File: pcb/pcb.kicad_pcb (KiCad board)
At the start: 2 copper layers, 63.8 x 43.2 mm, 34 parts, among them J1 BAT+, J10 GRN, J11 RED, J12 Load Cell, J2 BAT-, J3 Battery, J4 DS18B20, J5 TMP+, J6 TMPO, J7 TMP-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

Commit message: pcb-1.0.0-rc.4
Just a few final tweaks—labeling, adding a capacitor across USB
in for filtering.
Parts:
- added ?: , Symbols:OSHW-Logo2_7.3x6mm_SilkScreen, B.Cu at (125.2, 97.3)
- added C6: 1uF, Capacitors_SMD:C_0805, F.Cu at (142.1, 73.8)
- renumbered U1 to CN1, U3 to CN2, U4 to CN3, U5 to U1
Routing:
- net /USB+: track 77.3 -> 78.9 mm
- net /GND: track 65.9 -> 66.9 mm, vias 13 -> 14
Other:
- board text added: "1.0.0-rc.4"
- board text removed: "1.0.0-rc.3"
- board text removed: "OSHW"

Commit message: More capacitance! More ground pour!
Per recommendations. The ADC trace is long and very low-current,
and needs some smoothing for EMI reasons. The ground pour is bigger
to reduce the number of long traces to ground.
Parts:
- added C7: 100nF, Capacitors_SMD:C_0805, F.Cu at (141.1, 97.8)
- C6: value 1uF -> 100nF
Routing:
- net /GND: track 66.9 -> 52.1 mm, vias 14 -> 16
- net /ADC: track 48.3 -> 49.5 mm
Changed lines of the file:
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@@
 (kicad_pcb (version 4) (host pcbnew 4.0.7-e2-6376~58~ubuntu16.04.1)
   (general
-    (links 68)
+    (links 70)
     (no_connects 0)
-    (area 99.863999 58.638 182.188 114.438001)
+    (area 106.162999 65.462999 170.113001 108.813001)
     (thickness 1.6)
     (drawings 21)
-    (tracks 388)
+    (tracks 394)
     (zones 0)
-    (modules 36)
+    (modules 37)
     (nets 25)
   )
@@
       (effects (font (size 1 1) (thickness 0.15)))
     )
-    (fp_text value 1uF (at 5.207 0 270) (layer F.SilkS)
+    (fp_text value 100nF (at 5.842 0 270) (layer F.SilkS)
       (effects (font (size 1 1) (thickness 0.15)))
     )
@@
       (xy -0.113933 2.757629) (xy -0.013056 2.757714) (xy 0 2.757714) (xy 0.10391 2.757652)) (layer B.SilkS) (width 0.01))
   )
+  (module Capacitors_SMD:C_0805 (layer F.Cu)
+    (at 141.097 97.79 90)
+    (descr "Capacitor SMD 0805, reflow soldering, AVX (see smccp.pdf)")
+    (tags "capacitor 0805")
+    (attr smd)
+    (fp_text reference C7 (at 0.381 2.032 180) (layer F.SilkS)
+      (effects (font (size 1 1) (thickness 0.15)))
+    )
+    (fp_text value 100nF (at 1.905 3.429 180) (layer F.SilkS)
+      (effects (font (size 1 1) (thickness 0.15)))
+    )
+    (fp_text user %R (at 0.381 2.032 180) (layer F.Fab)
+      (effects (font (size 1 1) (thickness 0.15)))
+    )
+    (fp_line (start -1 0.62) (end -1 -0.62) (layer F.Fab) (width 0.1))
+    (fp_line (start 1 0.62) (end -1 0.62) (layer F.Fab) (width 0.1))
+    (fp_line (start 1 -0.62) (end 1 0.62) (layer F.Fab) (width 0.1))
+    (fp_line (start -1 -0.62) (end 1 -0.62) (layer F.Fab) (width 0.1))
+    (fp_line (start 0.5 -0.85) (end -0.5 -0.85) (layer F.SilkS) (width 0.12))
+    (fp_line (start -0.5 0.85) (end 0.5 0.85) (layer F.SilkS) (width 0.12))
+    (fp_line (start -1.75 -0.88) (end 1.75 -0.88) (layer F.CrtYd) (width 0.05))
+    (fp_line (start -1.75 -0.88) (end -1.75 0.87) (layer F.CrtYd) (width 0.05))
+    (fp_line (start 1.75 0.87) (end 1.75 -0.88) (layer F.CrtYd) (width 0.05))
+    (fp_line (start 1.75 0.87) (end -1.75 0.87) (layer F.CrtYd) (width 0.05))
+    (pad 1 smd rect (at -1 0 90) (size 1 1.25) (layers F.Cu F.Paste F.Mask)
+      (net 13 /ADC))
+    (pad 2 smd rect (at 1 0 90) (size 1 1.25) (layers F.Cu F.Paste F.Mask)
+      (net 9 /GND))
+    (model Capacitors_SMD.3dshapes/C_0805.wrl
+      (at (xyz 0 0 0))
+      (scale (xyz 1 1 1))
+      (rotate (xyz 0 0 0))
+    )
+  )
   (gr_text - (at 135.128 83.566) (layer F.SilkS)
     (effects (font (size 1.5 1.5) (thickness 0.3)) (justify mirror))
@@
   (segment (start 136.636 95.996) (end 138.938 98.298) (width 0.4) (layer F.Cu) (net 8))
   (segment (start 141.108 105.416) (end 141.108 105.294) (width 0.4) (layer F.Cu) (net 8))
+  (segment (start 138.684 93.996) (end 138.795 93.996) (width 0.25) (layer F.Cu) (net 9) (status C00000))
+  (segment (start 138.795 93.996) (end 139.7 93.091) (width 0.25) (layer F.Cu) (net 9) (status 400000))
+  (via (at 139.7 93.091) (size 0.6) (drill 0.4) (layers F.Cu B.Cu) (net 9))
+  (segment (start 150.556 100.838) (end 150.876 100.838) (width 0.25) (layer F.Cu) (net 9) (status C00000))
+  (segment (start 150.876 100.838) (end 151.384 100.33) (width 0.25) (layer F.Cu) (net 9) (status 400000))
+  (via (at 151.384 100.33) (size 0.6) (drill 0.4) (layers F.Cu B.Cu) (net 9))
+  (segment (start 141.097 96.79) (end 139.938 96.79) (width 0.25) (layer F.Cu) (net 9))
+  (via (at 139.827 96.901) (size 0.6) (drill 0.4) (layers F.Cu B.Cu) (net 9))
+  (segment (start 139.938 96.79) (end 139.827 96.901) (width 0.25) (layer F.Cu) (net 9))
   (segment (start 142.113 72.787) (end 142.113 71.755) (width 0.4) (layer F.Cu) (net 9))
   (via (at 142.113 71.755) (size 0.6) (drill 0.4) (layers F.Cu B.Cu) (net 9))
@@
   (segment (start 133.669 107.618) (end 133.858 107.807) (width 0.4) (layer F.Cu) (net 9))
   (segment (start 138.684 93.996) (end 138.728 93.996) (width 0.4) (layer F.Cu) (net 9))
-  (segment (start 138.728 93.996) (end 141.108 91.616) (width 0.4) (layer F.Cu) (net 9))
   (segment (start 131.064 107.618) (end 131.142 107.618) (width 0.4) (layer F.Cu) (net 9))
   (via (at 132.207 106.553) (size 0.6) (drill 0.4) (layers F.Cu B.Cu) (net 9))
@@
   (segment (start 121.793 84.074) (end 121.793 85.156) (width 0.4) (layer F.Cu) (net 9) (status 20))
   (via (at 121.793 84.074) (size 0.6) (drill 0.4) (layers F.Cu B.Cu) (net 9))
-  (segment (start 150.556 100.838) (end 151.638 100.838) (width 0.25) (layer F.Cu) (net 9) (status 10))
-  (segment (start 140.081 99.949) (end 137.922 99.949) (width 0.25) (layer B.Cu) (net 9))
-  (segment (start 140.97 100.838) (end 140.081 99.949) (width 0.25) (layer B.Cu) (net 9))
-  (segment (start 151.638 100.838) (end 140.97 100.838) (width 0.25) (layer B.Cu) (net 9))
-  (via (at 151.638 100.838) (size 0.6) (drill 0.4) (layers F.Cu B.Cu) (net 9))
   (segment (start 126 99.314) (end 125.349 99.314) (width 0.4) (layer F.Cu) (net 9) (status 10))
   (via (at 124.968 98.933) (size 0.6) (drill 0.4) (layers F.Cu B.Cu) (net 9))
@@
   (via (at 118.872 93.218) (size 0.6) (drill 0.4) (layers F.Cu B.Cu) (net 12))
   (segment (start 120.396 93.218) (end 118.872 93.218) (width 0.25) (layer B.Cu) (net 12))
+  (segment (start 141.605 99.822) (end 141.605 99.298) (width 0.25) (layer F.Cu) (net 13))
+  (segment (start 141.605 99.298) (end 141.097 98.79) (width 0.25) (layer F.Cu) (net 13))
   (segment (start 145.857 100.838) (end 145.857 100.518) (width 0.25) (layer F.Cu) (net 13) (status 30))
   (segment (start 145.857 100.518) (end 145.161 99.822) (width 0.25) (layer F.Cu) (net 13) (status 10))
-  (segment (start 145.161 99.822) (end 140.589 99.822) (width 0.25) (layer F.Cu) (net 13))
+  (segment (start 145.161 99.822) (end 141.605 99.822) (width 0.25) (layer F.Cu) (net 13))
+  (segment (start 141.605 99.822) (end 140.589 99.822) (width 0.25) (layer F.Cu) (net 13))
   (segment (start 119.253 105.537) (end 113.0935 105.537) (width 0.25) (layer B.Cu) (net 13))
   (segment (start 113.0935 105.537) (end 111.8235 104.267) (width 0.25) (layer B.Cu) (net 13))
@@
     (polygon
       (pts
-        (xy 165.989 82.296) (xy 165.989 93.091) (xy 162.179 93.091) (xy 162.179 91.694) (xy 143.51 91.694)
-        (xy 142.24 93.218) (xy 139.954 95.758) (xy 138.303 97.409) (xy 138.303 101.6) (xy 138.303 107.061)
-        (xy 129.032 107.061) (xy 123.571 101.6) (xy 112.522 101.6) (xy 112.522 98.806) (xy 112.522 69.088)
-        (xy 143.51 69.088)
+        (xy 165.989 82.296) (xy 165.989 93.091) (xy 165.989 100.711) (xy 138.303 100.711) (xy 138.303 107.061)
+        (xy 129.032 107.061) (xy 123.571 101.6) (xy 112.522 101.6) (xy 112.522 69.088) (xy 143.51 69.088)
       )
     )

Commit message: pcb-1.0.0-rc.5, blog post
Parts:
- added H1: MountingHole_2.2mm_M2, Mounting_Holes:MountingHole_2.2mm_M2, F.Cu at (114.8, 68.1)
- added H2: MountingHole_2.2mm_M2, Mounting_Holes:MountingHole_2.2mm_M2, F.Cu at (167.5, 106.2)
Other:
- board text added: "1.0.0-rc.5"
- board text removed: "1.0.0-rc.4"
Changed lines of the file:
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@@
     (tracks 394)
     (zones 0)
-    (modules 37)
+    (modules 39)
     (nets 25)
   )
@@
   (title_block
     (title "Pendulum PCB")
-    (date 2018-06-25)
-    (rev 1.0.0-rc.4)
+    (date 2018-06-26)
+    (rev 1.0.0-rc.5)
   )
   (layers
@@
     (add_net "Net-(R6-Pad2)")
     (add_net "Net-(R7-Pad2)")
+  )
+  (module Mounting_Holes:MountingHole_2.2mm_M2 (layer F.Cu)
+    (at 167.513 106.172)
+    (descr "Mounting Hole 2.2mm, no annular, M2")
+    (tags "mounting hole 2.2mm no annular m2")
+    (fp_text reference H2 (at 0 -2.159) (layer F.SilkS)
+      (effects (font (size 1 1) (thickness 0.15)))
+    )
+    (fp_text value MountingHole_2.2mm_M2 (at 0 3.2) (layer F.Fab)
+      (effects (font (size 1 1) (thickness 0.15)))
+    )
+    (fp_circle (center 0 0) (end 2.2 0) (layer Cmts.User) (width 0.15))
+    (fp_circle (center 0 0) (end 2.45 0) (layer F.CrtYd) (width 0.05))
+    (pad 1 np_thru_hole circle (at 0 0) (size 2.2 2.2) (drill 2.2) (layers *.Cu *.Mask))
   )
   (module Resistors_SMD:R_0805 (layer F.Cu)
@@
     )
   )
+  (module Mounting_Holes:MountingHole_2.2mm_M2 (layer F.Cu)
+    (at 114.808 68.072)
+    (descr "Mounting Hole 2.2mm, no annular, M2")
+    (tags "mounting hole 2.2mm no annular m2")
+    (fp_text reference H1 (at 0 2.286) (layer F.SilkS)
+      (effects (font (size 1 1) (thickness 0.15)))
+    )
+    (fp_text value MountingHole_2.2mm_M2 (at 0.254 -3.556) (layer F.Fab)
+      (effects (font (size 1 1) (thickness 0.15)))
+    )
+    (fp_circle (center 0 0) (end 2.2 0) (layer Cmts.User) (width 0.15))
+    (fp_circle (center 0 0) (end 2.45 0) (layer F.CrtYd) (width 0.05))
+    (pad 1 np_thru_hole circle (at 0 0) (size 2.2 2.2) (drill 2.2) (layers *.Cu *.Mask))
+  )
   (gr_text - (at 135.128 83.566) (layer F.SilkS)
     (effects (font (size 1.5 1.5) (thickness 0.3)) (justify mirror))
@@
     (arrow2b (pts (xy 100.138 111.738) (xy 101.264504 111.151579)))
   )
-  (gr_text 1.0.0-rc.4 (at 129.286 97.282 270) (layer B.SilkS)
+  (gr_text 1.0.0-rc.5 (at 129.286 97.282 270) (layer B.SilkS)
     (effects (font (size 1 1) (thickness 0.15)) (justify mirror))
   )
@@
   (segment (start 136.636 95.996) (end 138.938 98.298) (width 0.4) (layer F.Cu) (net 8))
   (segment (start 141.108 105.416) (end 141.108 105.294) (width 0.4) (layer F.Cu) (net 8))
-  (segment (start 138.684 93.996) (end 138.795 93.996) (width 0.25) (layer F.Cu) (net 9) (status C00000))
-  (segment (start 138.795 93.996) (end 139.7 93.091) (width 0.25) (layer F.Cu) (net 9) (status 400000))
+  (segment (start 138.684 93.996) (end 138.795 93.996) (width 0.25) (layer F.Cu) (net 9))
+  (segment (start 138.795 93.996) (end 139.7 93.091) (width 0.25) (layer F.Cu) (net 9))
   (via (at 139.7 93.091) (size 0.6) (drill 0.4) (layers F.Cu B.Cu) (net 9))
-  (segment (start 150.556 100.838) (end 150.876 100.838) (width 0.25) (layer F.Cu) (net 9) (status C00000))
-  (segment (start 150.876 100.838) (end 151.384 100.33) (width 0.25) (layer F.Cu) (net 9) (status 400000))
+  (segment (start 150.556 100.838) (end 150.876 100.838) (width 0.25) (layer F.Cu) (net 9))
+  (segment (start 150.876 100.838) (end 151.384 100.33) (width 0.25) (layer F.Cu) (net 9))
   (via (at 151.384 100.33) (size 0.6) (drill 0.4) (layers F.Cu B.Cu) (net 9))
   (segment (start 141.097 96.79) (end 139.938 96.79) (width 0.25) (layer F.Cu) (net 9))

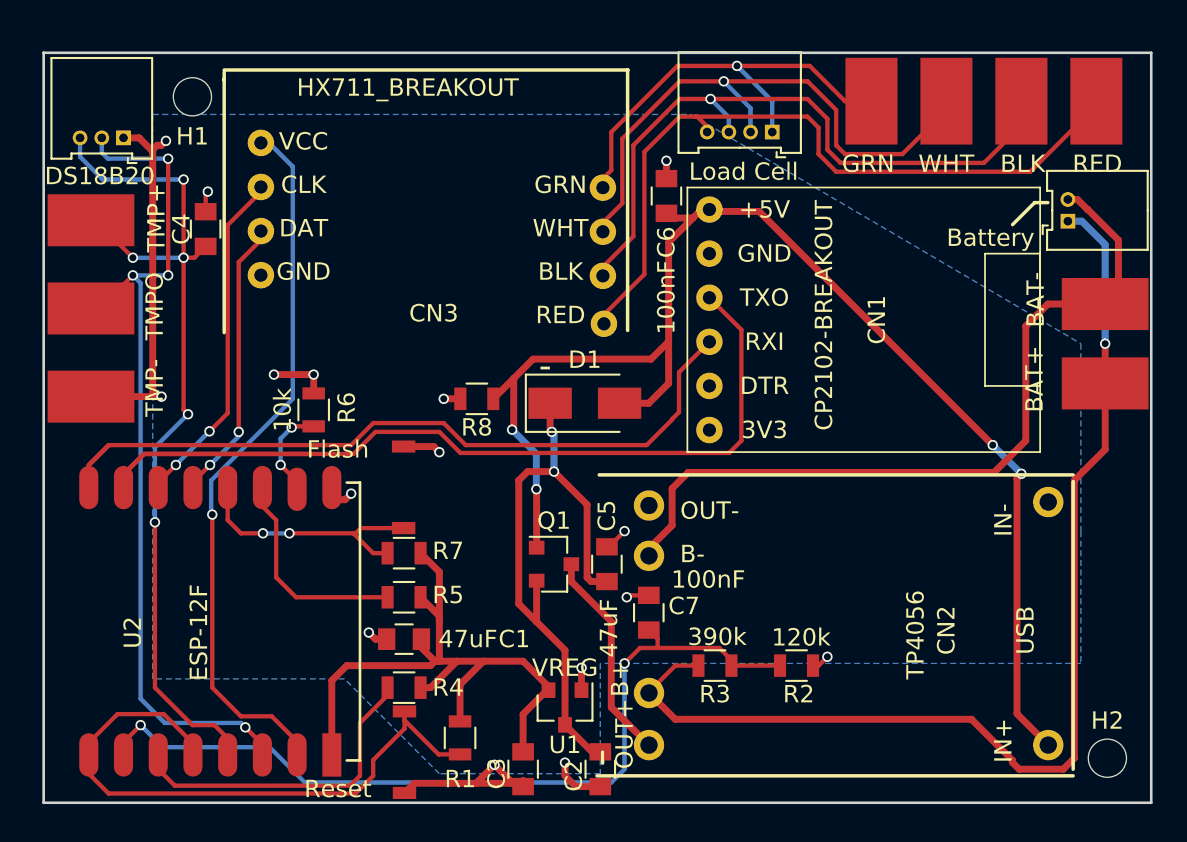
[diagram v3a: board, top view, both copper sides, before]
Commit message: Bite the bullet and go to a full-backside ground pour
This also involves removing some unnecessary vias and traces
routed on the back of the board. Where possible, power and signal
lines run over ground pour.
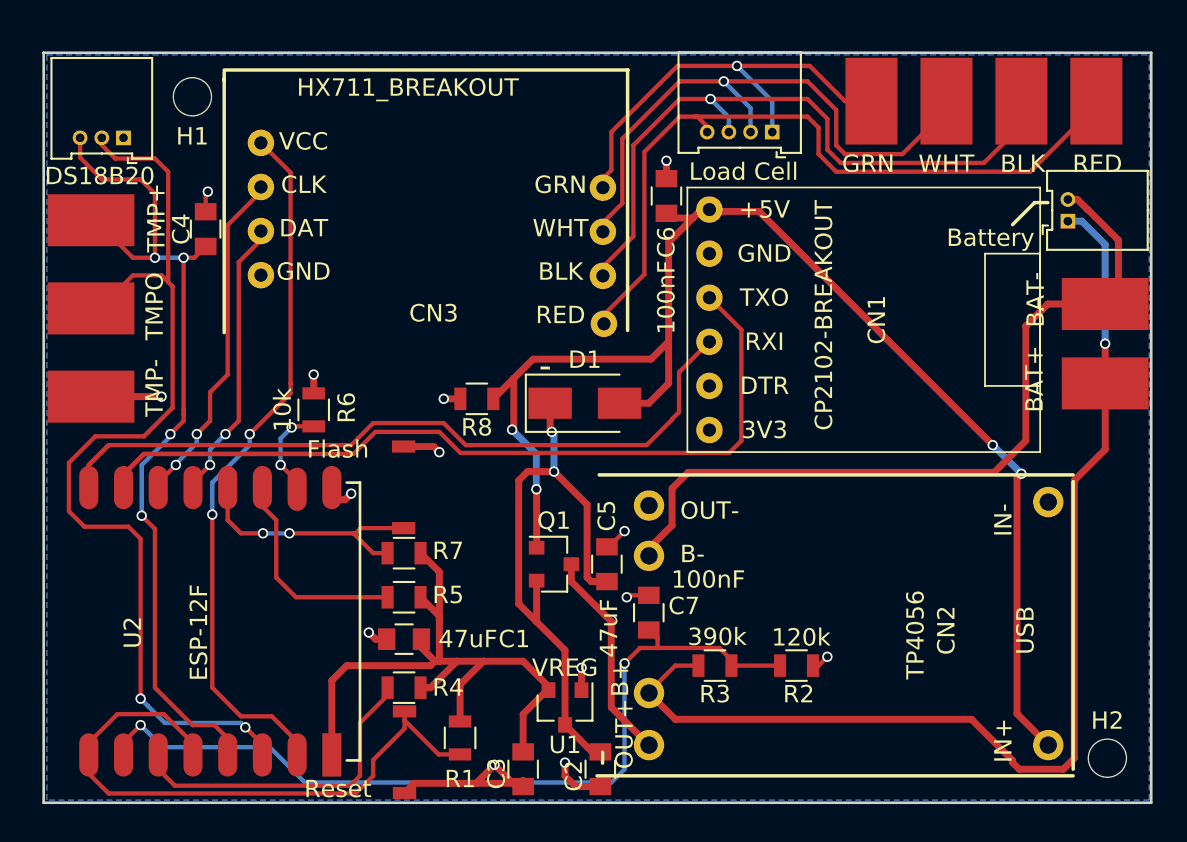
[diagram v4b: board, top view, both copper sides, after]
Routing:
- net /GND: track 52.1 -> 32.7 mm, vias 16 -> 14
- net /DSD: track 50.3 -> 57.0 mm, vias 4 -> 2
- net /DS+: track 51.4 -> 49.7 mm, vias 5 -> 4
- net /HX+: vias 1 -> 2

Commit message: Some further bottom trace reductions
Break up some islands in the pour so that the return paths are
closer to the traces.
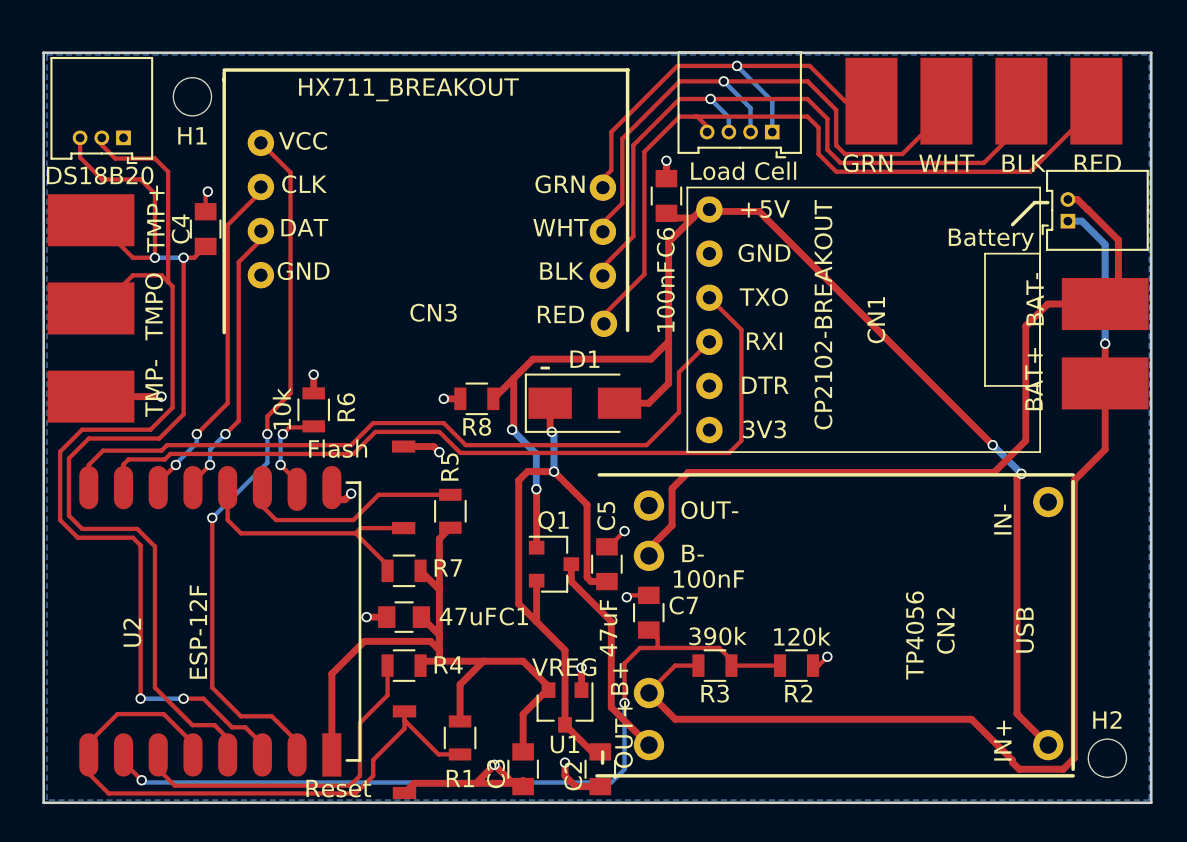
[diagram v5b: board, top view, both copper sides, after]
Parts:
- moved R5 5.63 mm to (129.7, 91.9), turned to 90 degrees
- moved R4 1.27 mm to (127.0, 100.8)
- moved C1 1.27 mm to (127.0, 98.0)
- moved R7 1.02 mm to (127.0, 95.4)
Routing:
- net /HostTX: track 59.2 -> 49.7 mm
- net /DS+: track 49.7 -> 57.4 mm, vias 4 -> 2
- net /HostRX: track 44.7 -> 43.1 mm
- net /DSD: track 57.0 -> 58.4 mm
- net Net-(R4-Pad1): track 19.5 -> 20.8 mm
- net /GND: track 32.7 -> 32.1 mm
- net Net-(R7-Pad2): track 14.2 -> 14.7 mm, vias 2 -> 0

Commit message: More grounding
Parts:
- moved R6 11.8 mm to (132.1, 91.9), turned to 90 degrees
- moved H2 7.62 mm to (167.4, 98.6)
- moved H1 0.25 mm to (115.1, 68.1)
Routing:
- net /DS+: track 57.4 -> 75.3 mm, vias 2 -> 0
- net Net-(R6-Pad2): track 6.28 -> 13.8 mm, vias 2 -> 0
- net /BAT+: track 64.1 -> 65.1 mm
- net Net-(R7-Pad2): track 14.7 -> 14.0 mm

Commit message: pcb-1.0.0-rc.6
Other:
- board text added: "1.0.0"
- board text removed: "1.0.0-rc.5"
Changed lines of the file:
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@@
     (links 70)
     (no_connects 0)
-    (area 106.162999 65.462999 170.113001 108.813001)
+    (area 99.863999 58.638 182.188 114.438001)
     (thickness 1.6)
     (drawings 21)
@@
   (title_block
     (title "Pendulum PCB")
-    (date 2018-06-26)
-    (rev 1.0.0-rc.5)
+    (date 2018-06-28)
+    (rev 1.0.0-rc.6)
   )
   (layers
     (0 F.Cu signal)
-    (31 B.Cu signal)
+    (31 B.Cu signal hide)
     (32 B.Adhes user)
     (33 F.Adhes user)
     (34 B.Paste user)
     (35 F.Paste user)
-    (36 B.SilkS user hide)
+    (36 B.SilkS user)
     (37 F.SilkS user)
     (38 B.Mask user)
@@
     (aux_axis_origin 11.938 11.938)
     (grid_origin 11.938 11.938)
-    (visible_elements FFFF7FBF)
+    (visible_elements FFFFFFBF)
     (pcbplotparams
       (layerselection 0x010f0_80000001)
@@
     (arrow2b (pts (xy 100.138 111.738) (xy 101.264504 111.151579)))
   )
-  (gr_text 1.0.0-rc.5 (at 129.286 97.282 270) (layer B.SilkS)
+  (gr_text 1.0.0 (at 129.286 97.282 270) (layer B.SilkS)
     (effects (font (size 1 1) (thickness 0.15)) (justify mirror))
   )
